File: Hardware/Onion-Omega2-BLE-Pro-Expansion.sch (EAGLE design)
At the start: 50 parts, among them J1 USB-MICROB, J2 USB-A-H, Q1 12Mhz 3225 Package

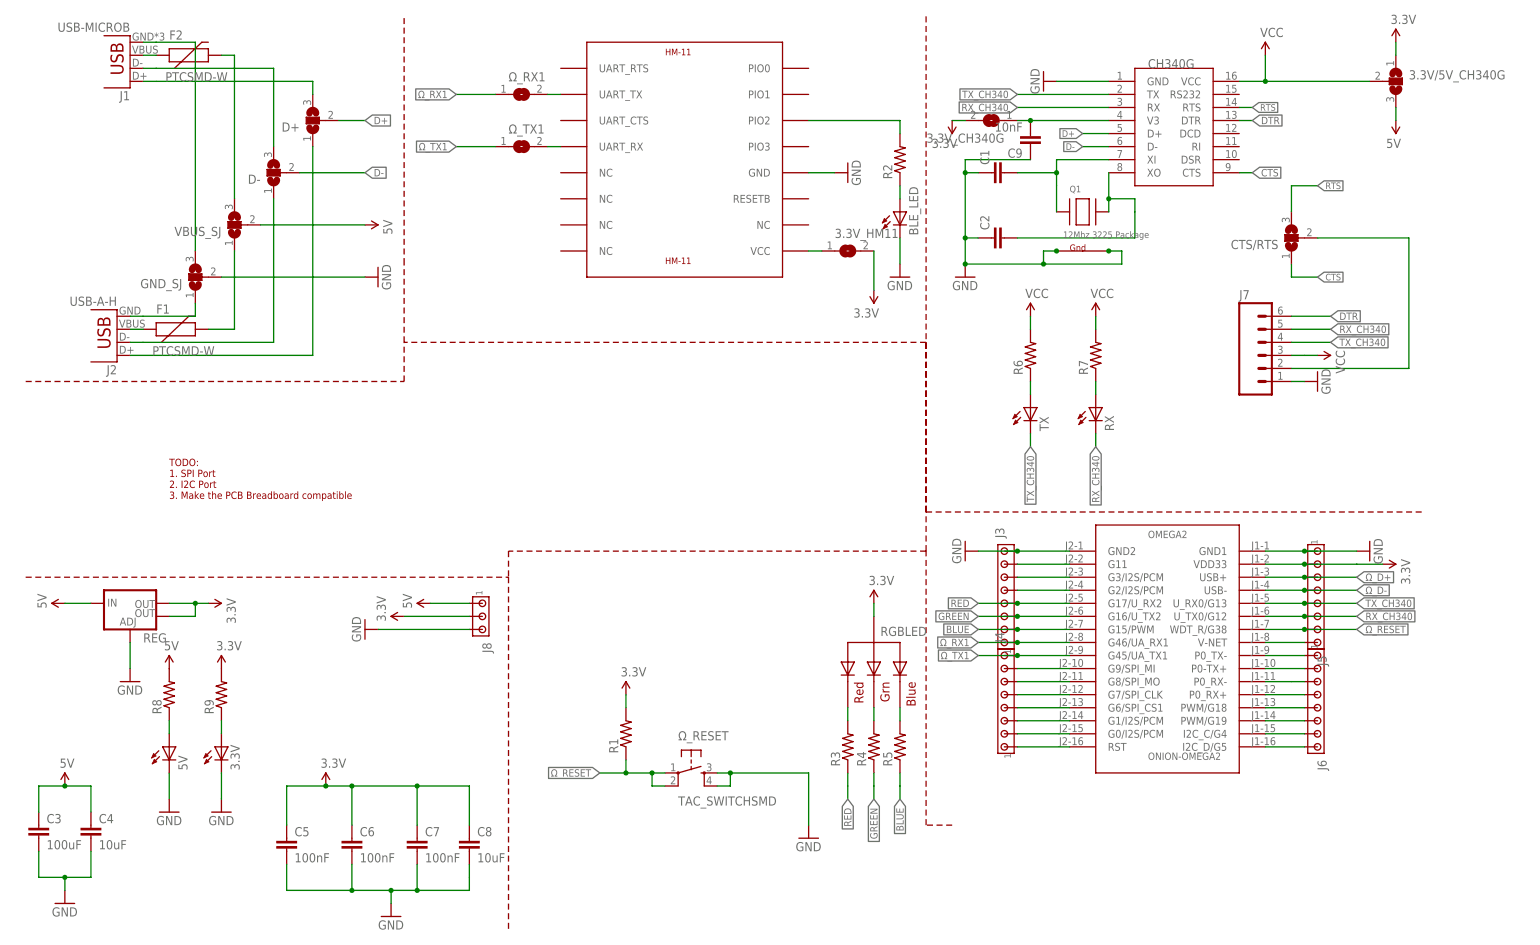
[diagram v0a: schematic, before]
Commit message: VBUS fused moved after jumper. Resistors for D+ and D- Lines. TODO: Reduce D+ line length
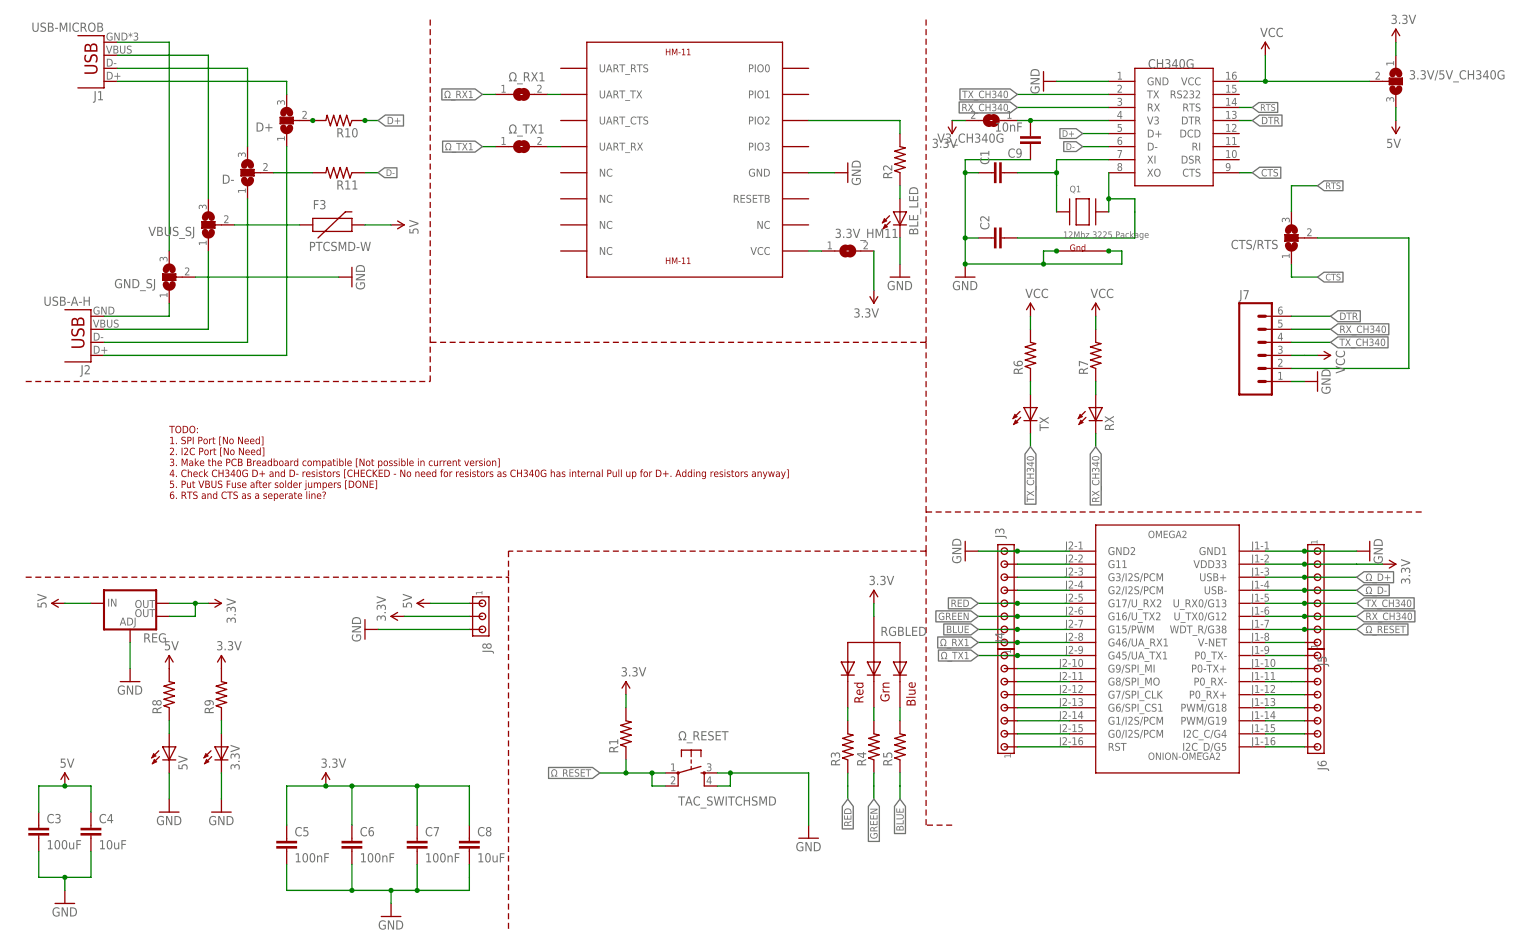
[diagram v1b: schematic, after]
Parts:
- removed F1, F2: PTCSMD-W, SparkFun-PowerIC:PTCSMD-W
- added F3: PTCSMD-W, SparkFun-PowerIC:PTCSMD-W
- added R10, R11: (no value), SparkFun-Passives:RESISTOR0805-RES
- renumbered 3.3V_CH340G to V3_CH340G
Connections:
- new net N$38: D+.2, R10.2
- net 5V: now also F3.2; no longer VBUS_SJ.2
- net D+: now also R10.1; no longer D+.2
- net D-: now also R11.1; no longer D-.2
- net N$27: now also F3.1, VBUS_SJ.2; no longer F2.1, J1.VBUS
- net N$37: now also VBUS_SJ.1; no longer F1.1
- net N$41: now also J1.VBUS; no longer F2.2
- net N$44: now also D-.2, R11.2; no longer F1.2, VBUS_SJ.1
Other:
- note added: "TODO: 1. SPI Port [No Need] 2. I2C Port [No Need] 3. Make the PCB Breadboard compatible [Not possible in current version] 4. Check CH340G D+ and D- resistors [CHECKED - No need for resistors as CH340G has internal Pull up for D+. Adding resistors anyway] 5. Put VBUS Fuse after solder jumpers [DONE] 6. RTS and CTS as a seperate line?"
- note removed: "TODO: 1. SPI Port 2. I2C Port 3. Make the PCB Breadboard compatible"
- moved on the sheet: D+, D-, GND_SJ, J1, J2, VBUS_SJ

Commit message: CTS and RTS lines seperated. Sent for production
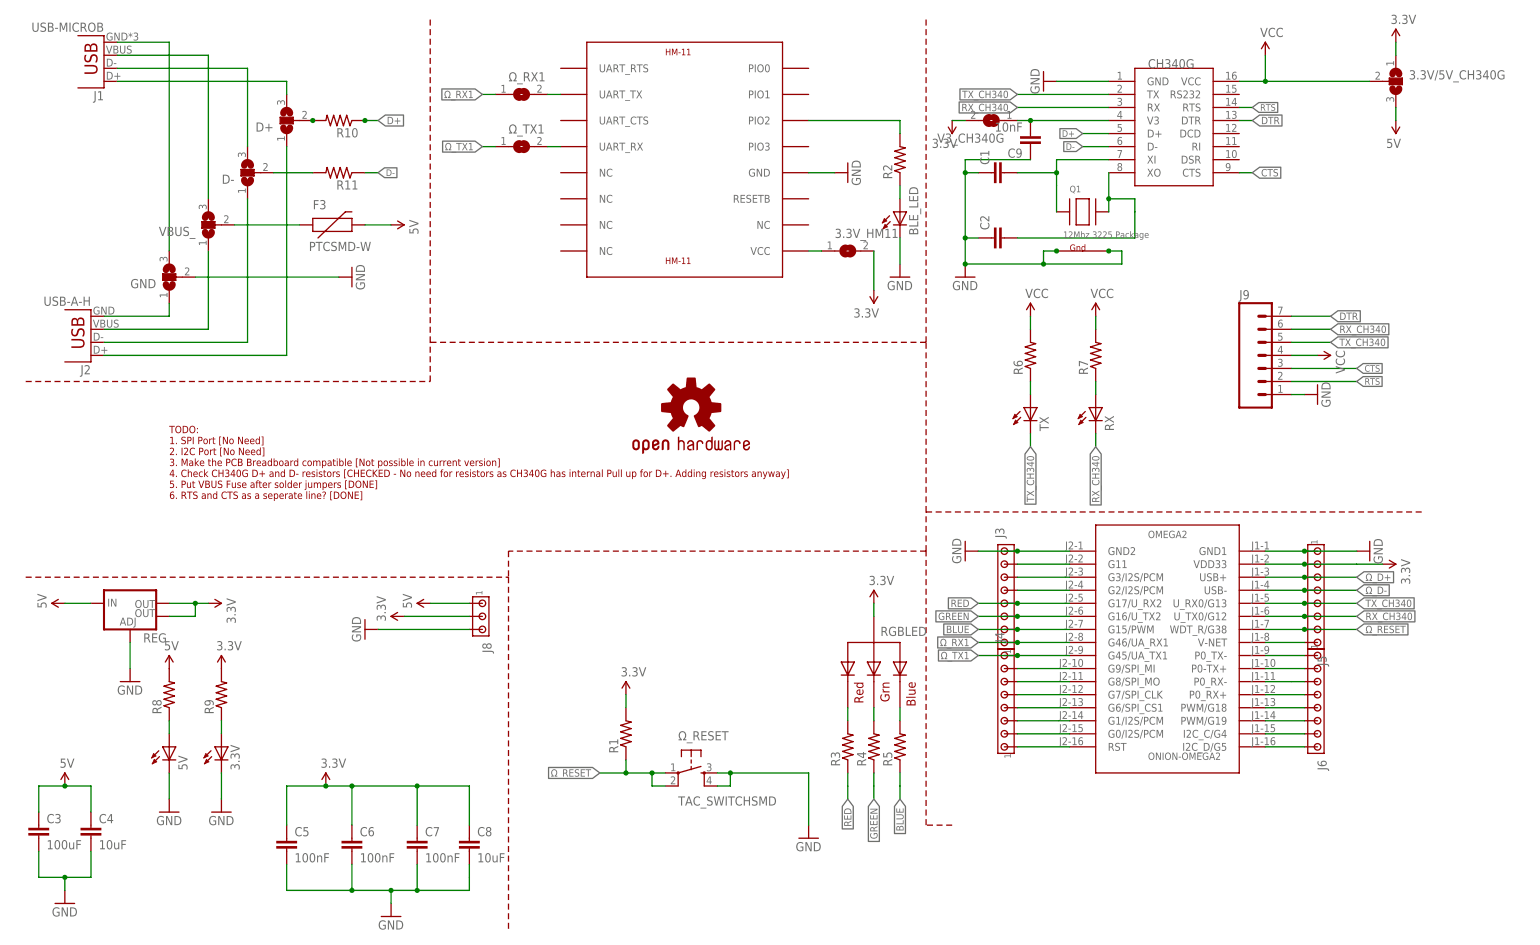
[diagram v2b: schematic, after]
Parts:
- removed CTS/RTS: (no value), jumper:SJ2W
- removed J7: (no value), SparkFun-Connectors:M06SMD-FEMALE-V2
- added J9: (no value), SparkFun-Connectors:M07SMD
- added LOGO1: OSHW-LOGOMINI, SparkFun-Aesthetics:OSHW-LOGOMINI
- renumbered GND_SJ to GND, VBUS_SJ to VBUS_
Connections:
- removed net N$48: CTS/RTS.2, J7.2
- net CTS: now also J9.3; no longer CTS/RTS.1
- net DTR: now also J9.7; no longer J7.6
- net GND: now also J9.1; no longer J7.1
- net RTS: now also J9.2; no longer CTS/RTS.3
- net RX_CH340: now also J9.6; no longer J7.5
- net TX_CH340: now also J9.5; no longer J7.4
- net VCC: now also J9.4; no longer J7.3
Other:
- note added: "TODO: 1. SPI Port [No Need] 2. I2C Port [No Need] 3. Make the PCB Breadboard compatible [Not possible in current version] 4. Check CH340G D+ and D- resistors [CHECKED - No need for resistors as CH340G has internal Pull up for D+. Adding resistors anyway] 5. Put VBUS Fuse after solder jumpers [DONE] 6. RTS and CTS as a seperate line? [DONE]"
- note removed: "TODO: 1. SPI Port [No Need] 2. I2C Port [No Need] 3. Make the PCB Breadboard compatible [Not possible in current version] 4. Check CH340G D+ and D- resistors [CHECKED - No need for resistors as CH340G has internal Pull up for D+. Adding resistors anyway] 5. Put VBUS Fuse after solder jumpers [DONE] 6. RTS and CTS as a seperate line?"
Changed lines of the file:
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@@
 <part name="D+" library="jumper" deviceset="SJ2W" device=""/>
 <part name="D-" library="jumper" deviceset="SJ2W" device=""/>
-<part name="VBUS_SJ" library="jumper" deviceset="SJ2W" device=""/>
-<part name="GND_SJ" library="jumper" deviceset="SJ2W" device=""/>
+<part name="VBUS_" library="jumper" deviceset="SJ2W" device=""/>
+<part name="GND" library="jumper" deviceset="SJ2W" device=""/>
 <part name="3.3V/5V_CH340G" library="jumper" deviceset="SJ2W" device=""/>
 <part name="VBUS3" library="SparkFun-Aesthetics" deviceset="5V" device=""/>
@@
 <part name="Q1" library="adafruit" deviceset="XTAL-4" device="-3225" value="12Mhz 3225 Package"/>
 <part name="C8" library="SparkFun-Passives" deviceset="CAP" device="1206" value="10uF"/>
-<part name="J7" library="SparkFun-Connectors" deviceset="M06" device="SMD-FEMALE-V2"/>
 <part name="SUPPLY9" library="SparkFun-Aesthetics" deviceset="VCC" device=""/>
 <part name="GND10" library="SparkFun-Aesthetics" deviceset="GND" device=""/>
@@
 <part name="VBUS5" library="SparkFun-Aesthetics" deviceset="5V" device=""/>
 <part name="SUPPLY14" library="SparkFun-Aesthetics" deviceset="3.3V" device=""/>
-<part name="CTS/RTS" library="jumper" deviceset="SJ2W" device=""/>
 <part name="R10" library="SparkFun-Passives" deviceset="RESISTOR" device="0805-RES"/>
 <part name="R11" library="SparkFun-Passives" deviceset="RESISTOR" device="0805-RES"/>
 <part name="F3" library="SparkFun-PowerIC" deviceset="PTC" device="SMD-W"/>
+<part name="J9" library="SparkFun-Connectors" deviceset="M07" device="SMD"/>
+<part name="LOGO1" library="SparkFun-Aesthetics" deviceset="OSHW-LOGO" device="MINI"/>
 </parts>
 <sheets>
@@
 4. Check CH340G D+ and D- resistors [CHECKED - No need for resistors as CH340G has internal Pull up for D+. Adding resistors anyway]
 5. Put VBUS Fuse after solder jumpers [DONE]
-6. RTS and CTS as a seperate line? </text>
+6. RTS and CTS as a seperate line? [DONE]</text>
 </plain>
 <instances>
@@
 <instance part="D+" gate="G$1" x="53.34" y="160.02" rot="R180"/>
 <instance part="D-" gate="G$1" x="45.72" y="149.86" rot="R180"/>
-<instance part="VBUS_SJ" gate="G$1" x="38.1" y="139.7" rot="R180"/>
-<instance part="GND_SJ" gate="G$1" x="30.48" y="129.54" rot="R180"/>
+<instance part="VBUS_" gate="G$1" x="38.1" y="139.7" rot="R180"/>
+<instance part="GND" gate="G$1" x="30.48" y="129.54" rot="R180"/>
 <instance part="3.3V/5V_CH340G" gate="G$1" x="269.24" y="167.64"/>
 <instance part="VBUS3" gate="G$1" x="269.24" y="160.02" rot="R180"/>
@@
 <instance part="Q1" gate="G$1" x="208.28" y="142.24"/>
 <instance part="C8" gate="G$1" x="88.9" y="17.78"/>
-<instance part="J7" gate="G$1" x="243.84" y="114.3"/>
 <instance part="SUPPLY9" gate="G$1" x="243.84" y="172.72"/>
-<instance part="GND10" gate="1" x="254" y="109.22" rot="R90"/>
+<instance part="GND10" gate="1" x="254" y="106.68" rot="R90"/>
 <instance part="SUPPLY10" gate="G$1" x="254" y="114.3" rot="R270"/>
 <instance part="Ω_RESET" gate="S" x="132.08" y="33.02"/>
@@
 <instance part="VBUS5" gate="G$1" x="30.48" y="53.34"/>
 <instance part="SUPPLY14" gate="G$1" x="40.64" y="53.34"/>
-<instance part="CTS/RTS" gate="G$1" x="248.92" y="137.16" rot="R180"/>
 <instance part="R10" gate="G$1" x="63.5" y="160.02" rot="R180"/>
 <instance part="R11" gate="G$1" x="63.5" y="149.86" rot="R180"/>
 <instance part="F3" gate="G$1" x="60.96" y="139.7"/>
+<instance part="J9" gate="G$1" x="243.84" y="111.76"/>
+<instance part="LOGO1" gate="G$1" x="132.08" y="104.14"/>
 </instances>
 <busses>
@@
 </segment>
 <segment>
-<pinref part="GND_SJ" gate="G$1" pin="2"/>
+<pinref part="GND" gate="G$1" pin="2"/>
 <pinref part="GND1" gate="1" pin="GND"/>
 <wire x1="63.5" y1="129.54" x2="35.56" y2="129.54" width="0.1524" layer="91"/>
@@
 </segment>
 <segment>
-<pinref part="J7" gate="G$1" pin="1"/>
-<pinref part="GND10" gate="1" pin="GND"/>
-<wire x1="248.92" y1="109.22" x2="251.46" y2="109.22" width="0.1524" layer="91"/>
-</segment>
-<segment>
 <wire x1="88.9" y1="12.7" x2="88.9" y2="15.24" width="0.1524" layer="91"/>
 <pinref part="C8" gate="G$1" pin="2"/>
@@
 <wire x1="40.64" y1="33.02" x2="40.64" y2="27.94" width="0.1524" layer="91"/>
 </segment>
+<segment>
+<pinref part="J9" gate="G$1" pin="1"/>
+<pinref part="GND10" gate="1" pin="GND"/>
+<wire x1="248.92" y1="106.68" x2="251.46" y2="106.68" width="0.1524" layer="91"/>
+</segment>
 </net>
 <net name="D+" class="0">
@@
 </segment>
 <segment>
-<pinref part="J7" gate="G$1" pin="5"/>
 <wire x1="248.92" y1="119.38" x2="256.54" y2="119.38" width="0.1524" layer="91"/>
 <label x="256.54" y="119.38" size="1.4224" layer="95" xref="yes"/>
+<pinref part="J9" gate="G$1" pin="6"/>
 </segment>
 <segment>
@@
 </segment>
 <segment>
-<pinref part="J7" gate="G$1" pin="4"/>
 <wire x1="248.92" y1="116.84" x2="256.54" y2="116.84" width="0.1524" layer="91"/>
 <label x="256.54" y="116.84" size="1.4224" layer="95" xref="yes"/>
+<pinref part="J9" gate="G$1" pin="5"/>
 </segment>
 <segment>
@@
 <segment>
 <pinref part="J2" gate="G$1" pin="GND"/>
-<pinref part="GND_SJ" gate="G$1" pin="1"/>
+<pinref part="GND" gate="G$1" pin="1"/>
 <wire x1="17.78" y1="121.92" x2="30.48" y2="121.92" width="0.1524" layer="91"/>
 <wire x1="30.48" y1="121.92" x2="30.48" y2="124.46" width="0.1524" layer="91"/>
@@
 <segment>
 <pinref part="J1" gate="G$1" pin="GND"/>
-<pinref part="GND_SJ" gate="G$1" pin="3"/>
+<pinref part="GND" gate="G$1" pin="3"/>
 <wire x1="20.32" y1="175.26" x2="30.48" y2="175.26" width="0.1524" layer="91"/>
 <wire x1="30.48" y1="175.26" x2="30.48" y2="134.62" width="0.1524" layer="91"/>
@@
 <net name="N$41" class="0">
 <segment>
-<pinref part="VBUS_SJ" gate="G$1" pin="3"/>
+<pinref part="VBUS_" gate="G$1" pin="3"/>
 <wire x1="38.1" y1="172.72" x2="38.1" y2="144.78" width="0.1524" layer="91"/>
 <pinref part="J1" gate="G$1" pin="VBUS"/>
@@
 </segment>
 <segment>
-<pinref part="CTS/RTS" gate="G$1" pin="1"/>
-<wire x1="248.92" y1="132.08" x2="248.92" y2="129.54" width="0.1524" layer="91"/>
-<wire x1="248.92" y1="129.54" x2="254" y2="129.54" width="0.1524" layer="91"/>
-<label x="254" y="129.54" size="1.27" layer="95" xref="yes"/>
+<label x="261.62" y="111.76" size="1.27" layer="95" xref="yes"/>
+<pinref part="J9" gate="G$1" pin="3"/>
+<wire x1="248.92" y1="111.76" x2="261.62" y2="111.76" width="0.1524" layer="91"/>
 </segment>
 </net>
@@
 </segment>
 <segment>
-<pinref part="J7" gate="G$1" pin="6"/>
 <wire x1="248.92" y1="121.92" x2="256.54" y2="121.92" width="0.1524" layer="91"/>
 <label x="256.54" y="121.92" size="1.4224" layer="95" xref="yes"/>
+<pinref part="J9" gate="G$1" pin="7"/>
 </segment>
 </net>
@@
 </segment>
 <segment>
-<pinref part="J7" gate="G$1" pin="3"/>
-<wire x1="248.92" y1="114.3" x2="251.46" y2="114.3" width="0.1524" layer="91"/>
 <pinref part="SUPPLY10" gate="G$1" pin="VCC"/>
-<wire x1="251.46" y1="114.3" x2="254" y2="114.3" width="0.1524" layer="91"/>
+<wire x1="248.92" y1="114.3" x2="254" y2="114.3" width="0.1524" layer="91"/>
+<pinref part="J9" gate="G$1" pin="4"/>
 </segment>
 <segment>
@@
 <pinref part="J2" gate="G$1" pin="VBUS"/>
 <wire x1="38.1" y1="119.38" x2="38.1" y2="134.62" width="0.1524" layer="91"/>
-<pinref part="VBUS_SJ" gate="G$1" pin="1"/>
+<pinref part="VBUS_" gate="G$1" pin="1"/>
 <wire x1="17.78" y1="119.38" x2="38.1" y2="119.38" width="0.1524" layer="91"/>
 </segment>
@@
 </segment>
 <segment>
-<pinref part="CTS/RTS" gate="G$1" pin="3"/>
-<wire x1="248.92" y1="142.24" x2="248.92" y2="147.32" width="0.1524" layer="91"/>
-<wire x1="248.92" y1="147.32" x2="254" y2="147.32" width="0.1524" layer="91"/>
-<label x="254" y="147.32" size="1.27" layer="95" xref="yes"/>
-</segment>
-</net>
-<net name="N$48" class="0">
-<segment>
-<pinref part="CTS/RTS" gate="G$1" pin="2"/>
-<wire x1="254" y1="137.16" x2="271.78" y2="137.16" width="0.1524" layer="91"/>
-<wire x1="271.78" y1="137.16" x2="271.78" y2="111.76" width="0.1524" layer="91"/>
-<pinref part="J7" gate="G$1" pin="2"/>
-<wire x1="271.78" y1="111.76" x2="248.92" y2="111.76" width="0.1524" layer="91"/>
+<label x="261.62" y="109.22" size="1.27" layer="95" xref="yes"/>
+<pinref part="J9" gate="G$1" pin="2"/>
+<wire x1="261.62" y1="109.22" x2="248.92" y2="109.22" width="0.1524" layer="91"/>
 </segment>
 </net>
@@
 <net name="N$27" class="0">
 <segment>
-<pinref part="VBUS_SJ" gate="G$1" pin="2"/>
+<pinref part="VBUS_" gate="G$1" pin="2"/>
 <wire x1="43.18" y1="139.7" x2="55.88" y2="139.7" width="0.1524" layer="91"/>
 <pinref part="F3" gate="G$1" pin="1"/>
